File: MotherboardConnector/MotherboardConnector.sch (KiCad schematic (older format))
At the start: 9 parts

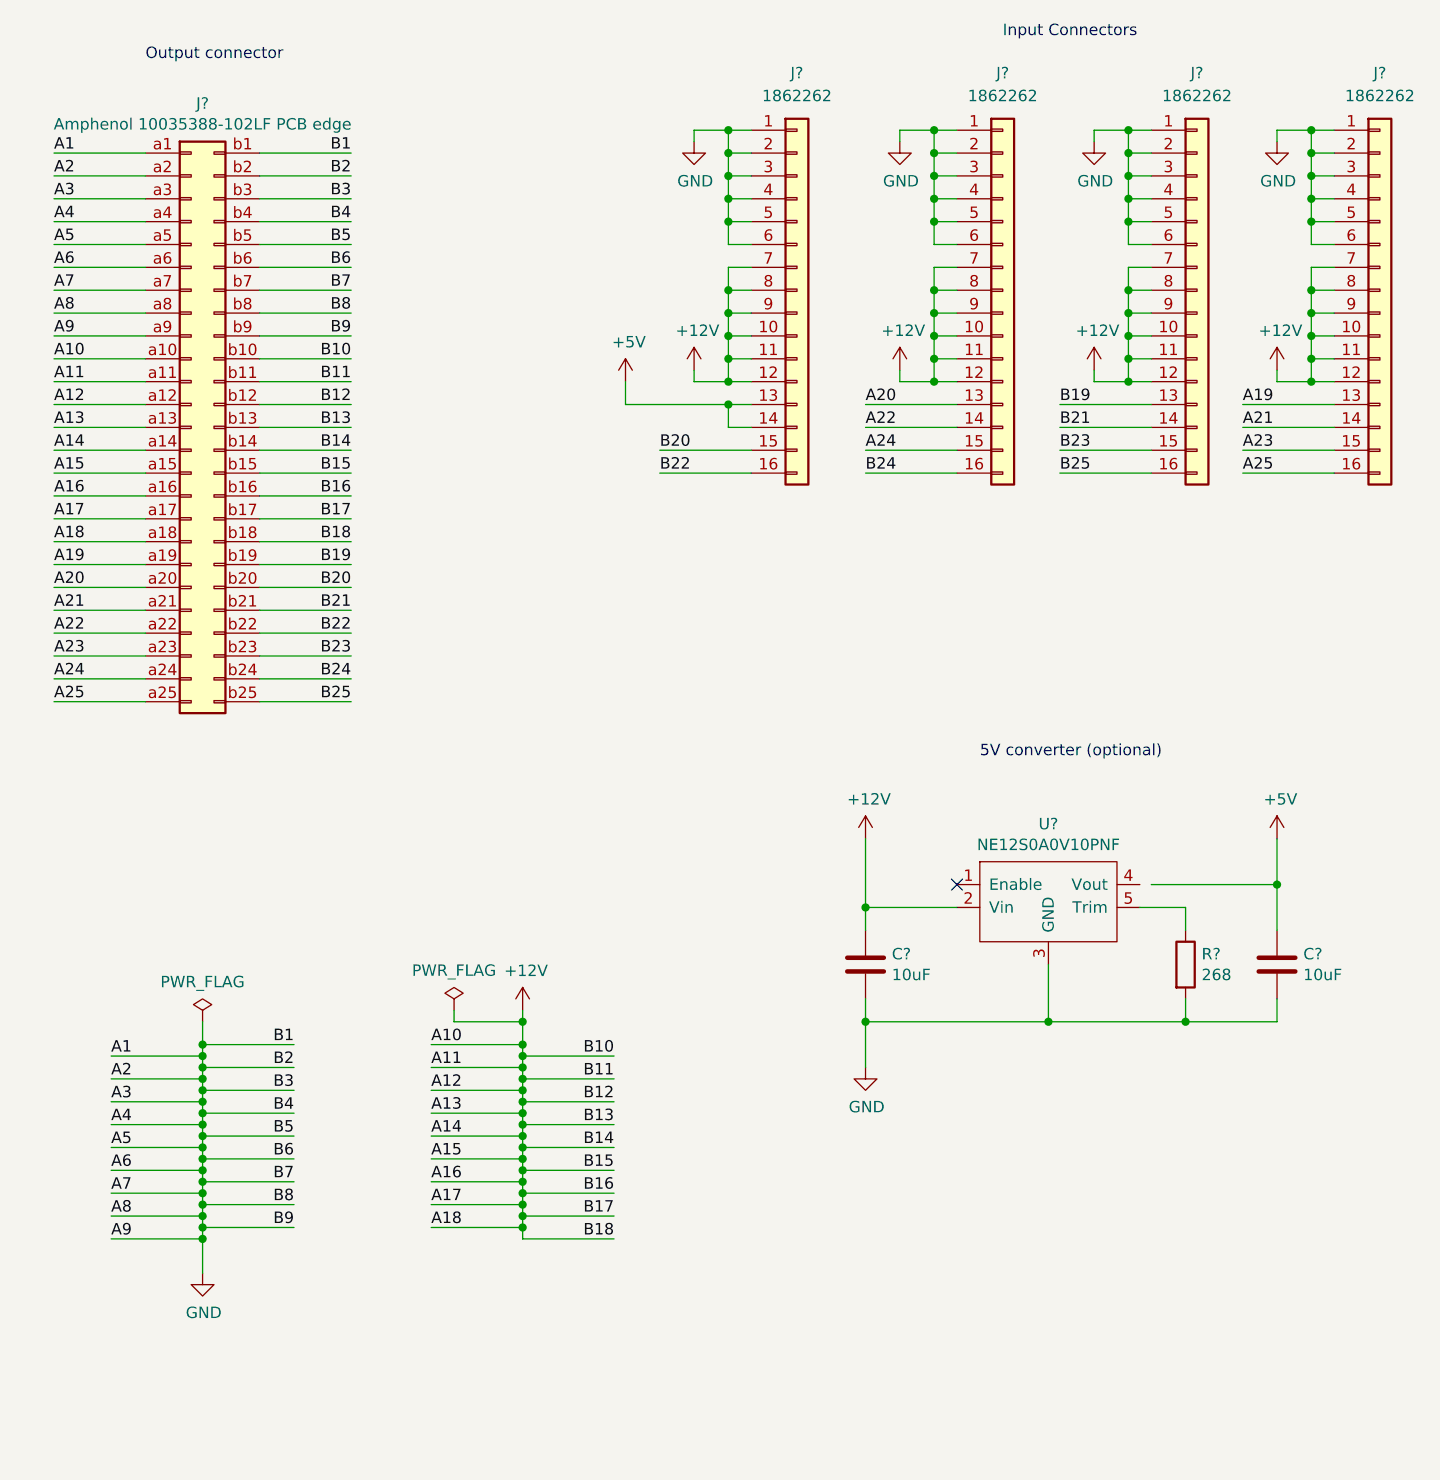
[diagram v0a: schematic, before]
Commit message: Motherboard connector PCB traces completed
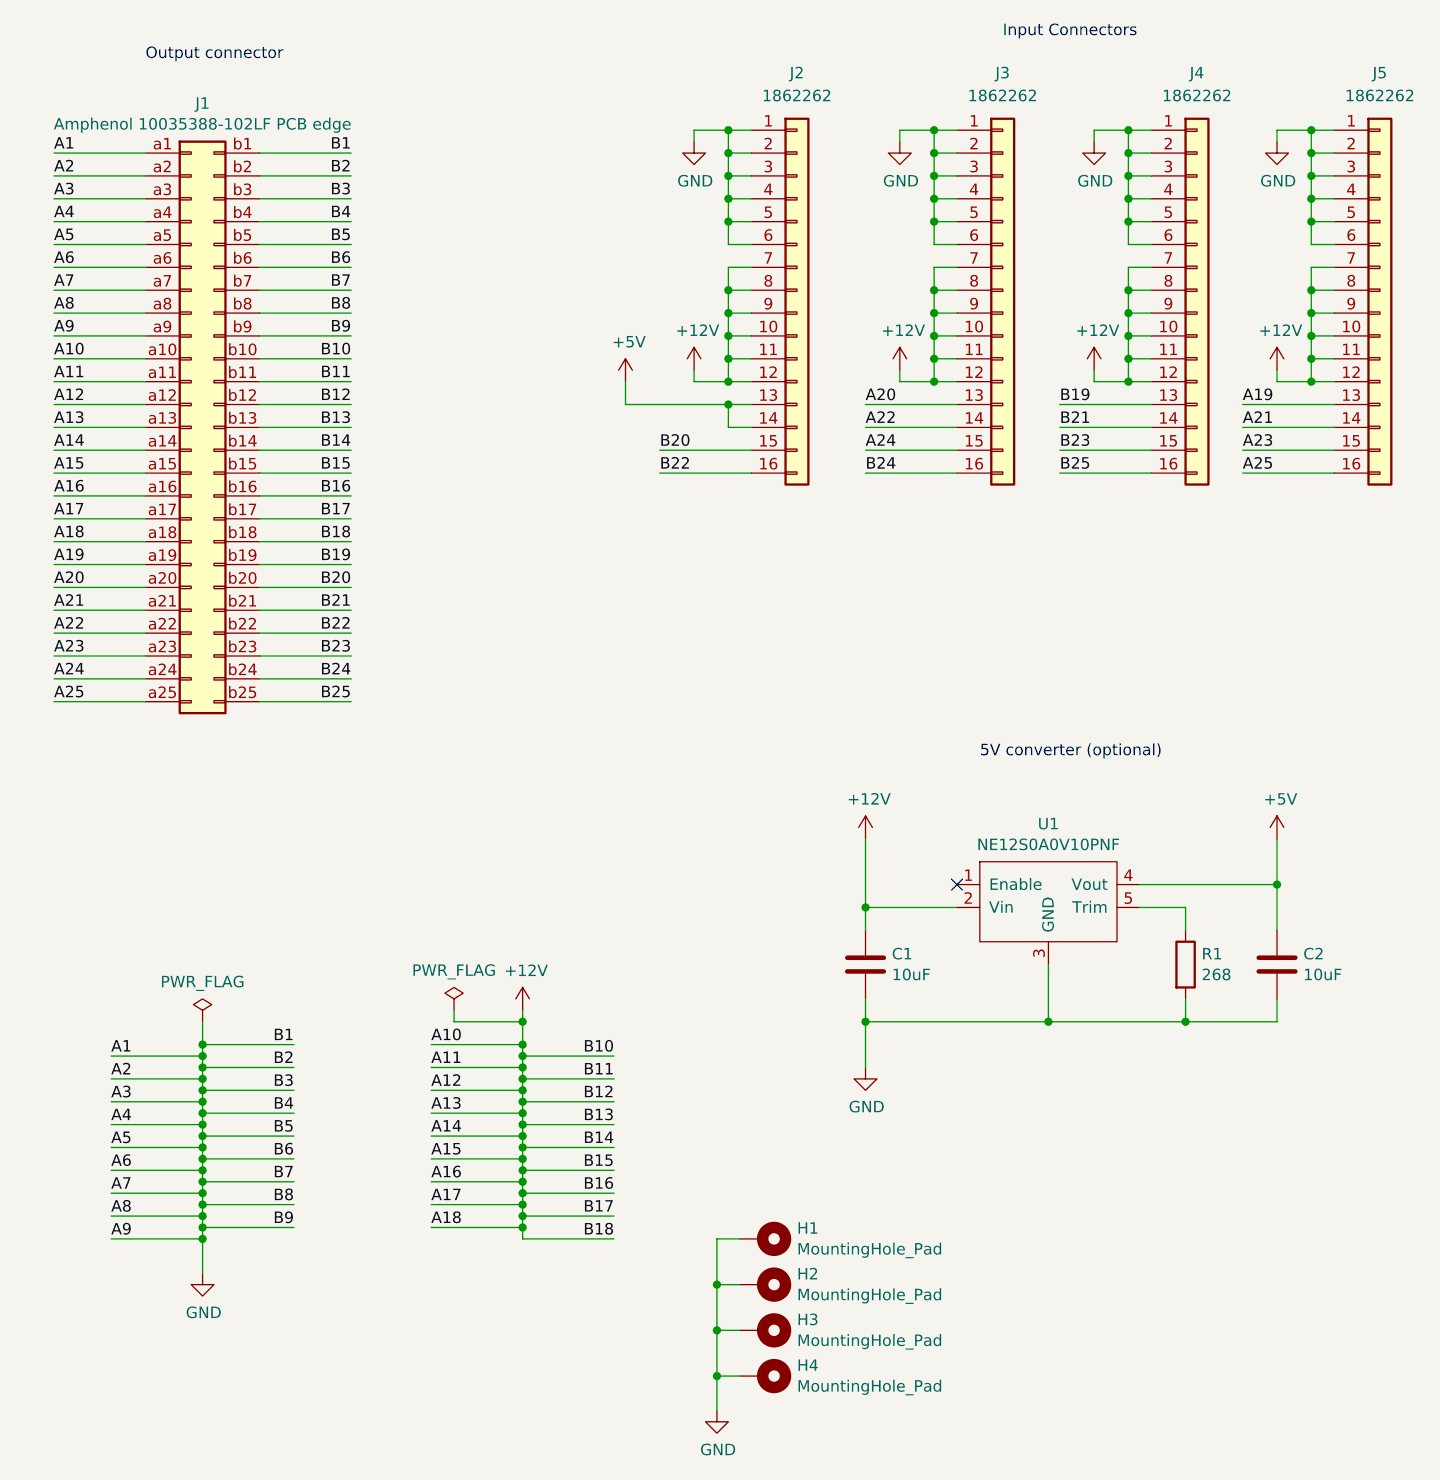
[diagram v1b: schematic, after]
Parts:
- added H1, H2, H3, H4: MountingHole_Pad, MountingHole:MountingHole_3.2mm_M3_Pad, symbol Mechanical:MountingHole_Pad
- C1, C2: renamed from C?; footprint (none) -> Capacitor_SMD:C_0603_1608Metric
- J1: renamed from J?; footprint (none) -> SupermicroConnectors:Amphenol_10035388-102LF_PCB_Edge
- J2, J3, J4, J5: renamed from J?; footprint (none) -> PhoenixContact:PhoenixContact1862262
- R1: renamed from R?; footprint (none) -> Resistor_SMD:R_0603_1608Metric
- U1: renamed from U?; footprint (none) -> Delta:Delta_NE12S0A0V10
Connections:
- net +5V: now also U1.4 (Vout)
- net GND: now also H1.1, H2.1, H3.1, H4.1
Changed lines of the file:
@@
 $EndDescr
 $Comp
-L Connector_Generic:Conn_02x25_Row_Letter_First J?
+L Connector_Generic:Conn_02x25_Row_Letter_First J1
 U 1 1 5C71EC9E
 P 2750 3000
-F 0 "J?" H 2800 4417 50  0000 C CNN
+F 0 "J1" H 2800 4417 50  0000 C CNN
 F 1 "Amphenol 10035388-102LF PCB edge" H 2800 4326 50  0000 C CNN
-F 2 "" H 2750 3000 50  0001 C CNN
+F 2 "SupermicroConnectors:Amphenol_10035388-102LF_PCB_Edge" H 2750 3000 50  0001 C CNN
 F 3 "~" H 2750 3000 50  0001 C CNN
 	1    2750 3000
@@
 	4200 6550 4600 6550
 $Comp
-L power:GND #PWR?
+L power:GND #PWR01
 U 1 1 5C11093C
 P 2800 6700
-F 0 "#PWR?" H 2800 6450 50  0001 C CNN
+F 0 "#PWR01" H 2800 6450 50  0001 C CNN
 F 1 "GND" H 2805 6527 50  0000 C CNN
 F 2 "" H 2800 6700 50  0001 C CNN
@@
 $EndComp
 $Comp
-L power:PWR_FLAG #FLG?
+L power:PWR_FLAG #FLG01
 U 1 1 5C110B13
 P 2800 5600
-F 0 "#FLG?" H 2800 5675 50  0001 C CNN
+F 0 "#FLG01" H 2800 5675 50  0001 C CNN
 F 1 "PWR_FLAG" H 2800 5774 50  0000 C CNN
 F 2 "" H 2800 5600 50  0001 C CNN
@@
 	2800 6500 2800 6550
 $Comp
-L power:PWR_FLAG #FLG?
+L power:PWR_FLAG #FLG02
 U 1 1 5C132E2D
 P 3900 5550
-F 0 "#FLG?" H 3900 5625 50  0001 C CNN
+F 0 "#FLG02" H 3900 5625 50  0001 C CNN
 F 1 "PWR_FLAG" H 3900 5724 50  0000 C CNN
 F 2 "" H 3900 5550 50  0001 C CNN
@@
 $EndComp
 $Comp
-L power:+12V #PWR?
+L power:+12V #PWR02
 U 1 1 5C132EA9
 P 4200 5550
-F 0 "#PWR?" H 4200 5400 50  0001 C CNN
+F 0 "#PWR02" H 4200 5400 50  0001 C CNN
 F 1 "+12V" H 4215 5723 50  0000 C CNN
 F 2 "" H 4200 5550 50  0001 C CNN
@@
 	4200 6450 4200 6500
 $Comp
-L Connector_Generic:Conn_01x16 J?
+L Connector_Generic:Conn_01x16 J2
 U 1 1 5C17DCF5
 P 5400 2400
-F 0 "J?" H 5400 3350 50  0000 C CNN
+F 0 "J2" H 5400 3350 50  0000 C CNN
 F 1 "1862262" H 5400 3250 50  0000 C CNN
-F 2 "" H 5400 2400 50  0001 C CNN
+F 2 "PhoenixContact:PhoenixContact1862262" H 5400 2400 50  0001 C CNN
 F 3 "~" H 5400 2400 50  0001 C CNN
 	1    5400 2400
@@
 $EndComp
 $Comp
-L Connector_Generic:Conn_01x16 J?
+L Connector_Generic:Conn_01x16 J3
 U 1 1 5C17DD8D
 P 6300 2400
-F 0 "J?" H 6300 3350 50  0000 C CNN
+F 0 "J3" H 6300 3350 50  0000 C CNN
 F 1 "1862262" H 6300 3250 50  0000 C CNN
-F 2 "" H 6300 2400 50  0001 C CNN
+F 2 "PhoenixContact:PhoenixContact1862262" H 6300 2400 50  0001 C CNN
 F 3 "~" H 6300 2400 50  0001 C CNN
 	1    6300 2400
@@
 $EndComp
 $Comp
-L Connector_Generic:Conn_01x16 J?
+L Connector_Generic:Conn_01x16 J4
 U 1 1 5C17DDDA
 P 7150 2400
-F 0 "J?" H 7150 3350 50  0000 C CNN
+F 0 "J4" H 7150 3350 50  0000 C CNN
 F 1 "1862262" H 7150 3250 50  0000 C CNN
-F 2 "" H 7150 2400 50  0001 C CNN
+F 2 "PhoenixContact:PhoenixContact1862262" H 7150 2400 50  0001 C CNN
 F 3 "~" H 7150 2400 50  0001 C CNN
 	1    7150 2400
@@
 $EndComp
 $Comp
-L Connector_Generic:Conn_01x16 J?
+L Connector_Generic:Conn_01x16 J5
 U 1 1 5C17DE4E
 P 7950 2400
-F 0 "J?" H 7950 3350 50  0000 C CNN
+F 0 "J5" H 7950 3350 50  0000 C CNN
 F 1 "1862262" H 7950 3250 50  0000 C CNN
-F 2 "" H 7950 2400 50  0001 C CNN
+F 2 "PhoenixContact:PhoenixContact1862262" H 7950 2400 50  0001 C CNN
 F 3 "~" H 7950 2400 50  0001 C CNN
 	1    7950 2400
@@
 	5100 2100 5100 2200
 $Comp
-L power:GND #PWR?
+L power:GND #PWR04
 U 1 1 5C1D5548
 P 4950 1750
-F 0 "#PWR?" H 4950 1500 50  0001 C CNN
+F 0 "#PWR04" H 4950 1500 50  0001 C CNN
 F 1 "GND" H 4955 1577 50  0000 C CNN
 F 2 "" H 4950 1750 50  0001 C CNN
@@
 	5100 2700 5100 2800
 $Comp
-L power:+12V #PWR?
+L power:+12V #PWR05
 U 1 1 5C218737
 P 4950 2750
-F 0 "#PWR?" H 4950 2600 50  0001 C CNN
+F 0 "#PWR05" H 4950 2600 50  0001 C CNN
 F 1 "+12V" H 4965 2923 50  0000 C CNN
 F 2 "" H 4950 2750 50  0001 C CNN
@@
 	6000 2100 6000 2200
 $Comp
-L power:GND #PWR?
+L power:GND #PWR08
 U 1 1 5C26010D
 P 5850 1750
-F 0 "#PWR?" H 5850 1500 50  0001 C CNN
+F 0 "#PWR08" H 5850 1500 50  0001 C CNN
 F 1 "GND" H 5855 1577 50  0000 C CNN
 F 2 "" H 5850 1750 50  0001 C CNN
@@
 	6000 2700 6000 2800
 $Comp
-L power:+12V #PWR?
+L power:+12V #PWR09
 U 1 1 5C260122
 P 5850 2750
-F 0 "#PWR?" H 5850 2600 50  0001 C CNN
+F 0 "#PWR09" H 5850 2600 50  0001 C CNN
 F 1 "+12V" H 5865 2923 50  0000 C CNN
 F 2 "" H 5850 2750 50  0001 C CNN
@@
 	6850 2100 6850 2200
 $Comp
-L power:GND #PWR?
+L power:GND #PWR010
 U 1 1 5C26EAF9
 P 6700 1750
-F 0 "#PWR?" H 6700 1500 50  0001 C CNN
+F 0 "#PWR010" H 6700 1500 50  0001 C CNN
 F 1 "GND" H 6705 1577 50  0000 C CNN
 F 2 "" H 6700 1750 50  0001 C CNN
@@
 	6850 2700 6850 2800
 $Comp
-L power:+12V #PWR?
+L power:+12V #PWR011
 U 1 1 5C26EB0E
 P 6700 2750
-F 0 "#PWR?" H 6700 2600 50  0001 C CNN
+F 0 "#PWR011" H 6700 2600 50  0001 C CNN
 F 1 "+12V" H 6715 2923 50  0000 C CNN
 F 2 "" H 6700 2750 50  0001 C CNN
@@
 	7650 2100 7650 2200
 $Comp
-L power:GND #PWR?
+L power:GND #PWR012
 U 1 1 5C280371
 P 7500 1750
-F 0 "#PWR?" H 7500 1500 50  0001 C CNN
+F 0 "#PWR012" H 7500 1500 50  0001 C CNN
 F 1 "GND" H 7505 1577 50  0000 C CNN
 F 2 "" H 7500 1750 50  0001 C CNN
@@
 	7650 2700 7650 2800
 $Comp
-L power:+12V #PWR?
+L power:+12V #PWR013
 U 1 1 5C280386
 P 7500 2750
-F 0 "#PWR?" H 7500 2600 50  0001 C CNN
+F 0 "#PWR013" H 7500 2600 50  0001 C CNN
 F 1 "+12V" H 7515 2923 50  0000 C CNN
 F 2 "" H 7500 2750 50  0001 C CNN
@@
 	5200 3200 4800 3200
 $Comp
-L NE12S0A0V10PNF:NE12S0A0V10PNF U?
+L NE12S0A0V10PNF:NE12S0A0V10PNF U1
 U 1 1 5C4F45DB
 P 6500 5300
-F 0 "U?" H 6500 5865 50  0000 C CNN
+F 0 "U1" H 6500 5865 50  0000 C CNN
 F 1 "NE12S0A0V10PNF" H 6500 5774 50  0000 C CNN
-F 2 "" H 6500 5300 50  0001 C CNN
+F 2 "Delta:Delta_NE12S0A0V10" H 6500 5300 50  0001 C CNN
 F 3 "" H 6500 5300 50  0001 C CNN
 	1    6500 5300
@@
 $EndComp
 $Comp
-L Device:R R?
+L Device:R R1
 U 1 1 5C50E3E1
 P 7100 5350
-F 0 "R?" H 7170 5396 50  0000 L CNN
+F 0 "R1" H 7170 5396 50  0000 L CNN
 F 1 "268" H 7170 5305 50  0000 L CNN
-F 2 "" V 7030 5350 50  0001 C CNN
+F 2 "Resistor_SMD:R_0603_1608Metric" V 7030 5350 50  0001 C CNN
 F 3 "~" H 7100 5350 50  0001 C CNN
 	1    7100 5350
@@
 $EndComp
 $Comp
-L Device:C C?
+L Device:C C2
 U 1 1 5C50E459
 P 7500 5350
-F 0 "C?" H 7615 5396 50  0000 L CNN
+F 0 "C2" H 7615 5396 50  0000 L CNN
 F 1 "10uF" H 7615 5305 50  0000 L CNN
-F 2 "" H 7538 5200 50  0001 C CNN
+F 2 "Capacitor_SMD:C_0603_1608Metric" H 7538 5200 50  0001 C CNN
 F 3 "~" H 7500 5350 50  0001 C CNN
 	1    7500 5350
@@
 $EndComp
 $Comp
-L power:GND #PWR?
+L power:GND #PWR07
 U 1 1 5C50E580
 P 5700 5800
-F 0 "#PWR?" H 5700 5550 50  0001 C CNN
+F 0 "#PWR07" H 5700 5550 50  0001 C CNN
 F 1 "GND" H 5705 5627 50  0000 C CNN
 F 2 "" H 5700 5800 50  0001 C CNN
@@
 $EndComp
 $Comp
-L power:+5V #PWR?
+L power:+5V #PWR014
 U 1 1 5C50E5E4
 P 7500 4800
-F 0 "#PWR?" H 7500 4650 50  0001 C CNN
+F 0 "#PWR014" H 7500 4650 50  0001 C CNN
 F 1 "+5V" H 7515 4973 50  0000 C CNN
 F 2 "" H 7500 4800 50  0001 C CNN
@@
 $EndComp
 $Comp
-L Device:C C?
+L Device:C C1
 U 1 1 5C50E64A
 P 5700 5350
-F 0 "C?" H 5815 5396 50  0000 L CNN
+F 0 "C1" H 5815 5396 50  0000 L CNN
 F 1 "10uF" H 5815 5305 50  0000 L CNN
-F 2 "" H 5738 5200 50  0001 C CNN
+F 2 "Capacitor_SMD:C_0603_1608Metric" H 5738 5200 50  0001 C CNN
 F 3 "~" H 5700 5350 50  0001 C CNN
 	1    5700 5350
@@
 $EndComp
 $Comp
-L power:+12V #PWR?
+L power:+12V #PWR06
 U 1 1 5C51B4AD
 P 5700 4800
-F 0 "#PWR?" H 5700 4650 50  0001 C CNN
+F 0 "#PWR06" H 5700 4650 50  0001 C CNN
 F 1 "+12V" H 5715 4973 50  0000 C CNN
 F 2 "" H 5700 4800 50  0001 C CNN
@@
 Wire Wire Line
 	7100 5100 7100 5200
-Wire Wire Line
-	6950 5000 7500 5000
 Wire Wire Line
 	7500 5000 7500 4800
@@
 5V converter (optional)
 $Comp
-L power:+5V #PWR?
+L power:+5V #PWR03
 U 1 1 5C60A1F7
 P 4650 2800
-F 0 "#PWR?" H 4650 2650 50  0001 C CNN
+F 0 "#PWR03" H 4650 2650 50  0001 C CNN
 F 1 "+5V" H 4665 2973 50  0000 C CNN
 F 2 "" H 4650 2800 50  0001 C CNN
@@
 	5700 5600 5700 5800
 Connection ~ 5700 5600
+Wire Wire Line
+	6900 5000 7500 5000
+$Comp
+L Mechanical:MountingHole_Pad H4
+U 1 1 5C215AB3
+P 5250 7150
+F 0 "H4" V 5204 7300 50  0000 L CNN
+F 1 "MountingHole_Pad" V 5295 7300 50  0000 L CNN
+F 2 "MountingHole:MountingHole_3.2mm_M3_Pad" H 5250 7150 50  0001 C CNN
+F 3 "~" H 5250 7150 50  0001 C CNN
+	1    5250 7150
+	0    1    1    0
+$EndComp
+$Comp
+L Mechanical:MountingHole_Pad H3
+U 1 1 5C225024
+P 5250 6950
+F 0 "H3" V 5204 7100 50  0000 L CNN
+F 1 "MountingHole_Pad" V 5295 7100 50  0000 L CNN
+F 2 "MountingHole:MountingHole_3.2mm_M3_Pad" H 5250 6950 50  0001 C CNN
+F 3 "~" H 5250 6950 50  0001 C CNN
+	1    5250 6950
+	0    1    1    0
+$EndComp
+$Comp
+L Mechanical:MountingHole_Pad H2
+U 1 1 5C2344DA
+P 5250 6750
+F 0 "H2" V 5204 6900 50  0000 L CNN
+F 1 "MountingHole_Pad" V 5295 6900 50  0000 L CNN
+F 2 "MountingHole:MountingHole_3.2mm_M3_Pad" H 5250 6750 50  0001 C CNN
+F 3 "~" H 5250 6750 50  0001 C CNN
+	1    5250 6750
+	0    1    1    0
+$EndComp
+$Comp
+L Mechanical:MountingHole_Pad H1
+U 1 1 5C2344E0
+P 5250 6550
+F 0 "H1" V 5204 6700 50  0000 L CNN
+F 1 "MountingHole_Pad" V 5295 6700 50  0000 L CNN
+F 2 "MountingHole:MountingHole_3.2mm_M3_Pad" H 5250 6550 50  0001 C CNN
+F 3 "~" H 5250 6550 50  0001 C CNN
+	1    5250 6550
+	0    1    1    0
+$EndComp
+$Comp
+L power:GND #PWR015
+U 1 1 5C2439CE
+P 5050 7300
+F 0 "#PWR015" H 5050 7050 50  0001 C CNN
+F 1 "GND" H 5055 7127 50  0000 C CNN
+F 2 "" H 5050 7300 50  0001 C CNN
+F 3 "" H 5050 7300 50  0001 C CNN
+	1    5050 7300
+	1    0    0    -1
+$EndComp
+Wire Wire Line
+	5150 6550 5050 6550
+Wire Wire Line
+	5050 6550 5050 6750
+Wire Wire Line
+	5150 6750 5050 6750
+Connection ~ 5050 6750
+Wire Wire Line
+	5050 6750 5050 6950
+Wire Wire Line
+	5150 6950 5050 6950
+Connection ~ 5050 6950
+Wire Wire Line
+	5050 6950 5050 7150
+Wire Wire Line
+	5150 7150 5050 7150
+Connection ~ 5050 7150
+Wire Wire Line
+	5050 7150 5050 7300
 $EndSCHEMATC
